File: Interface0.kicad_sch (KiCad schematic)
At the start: 5 parts, among them IC26 MC6821, U107 74LS138, U108 74LS04, U109 74LS11

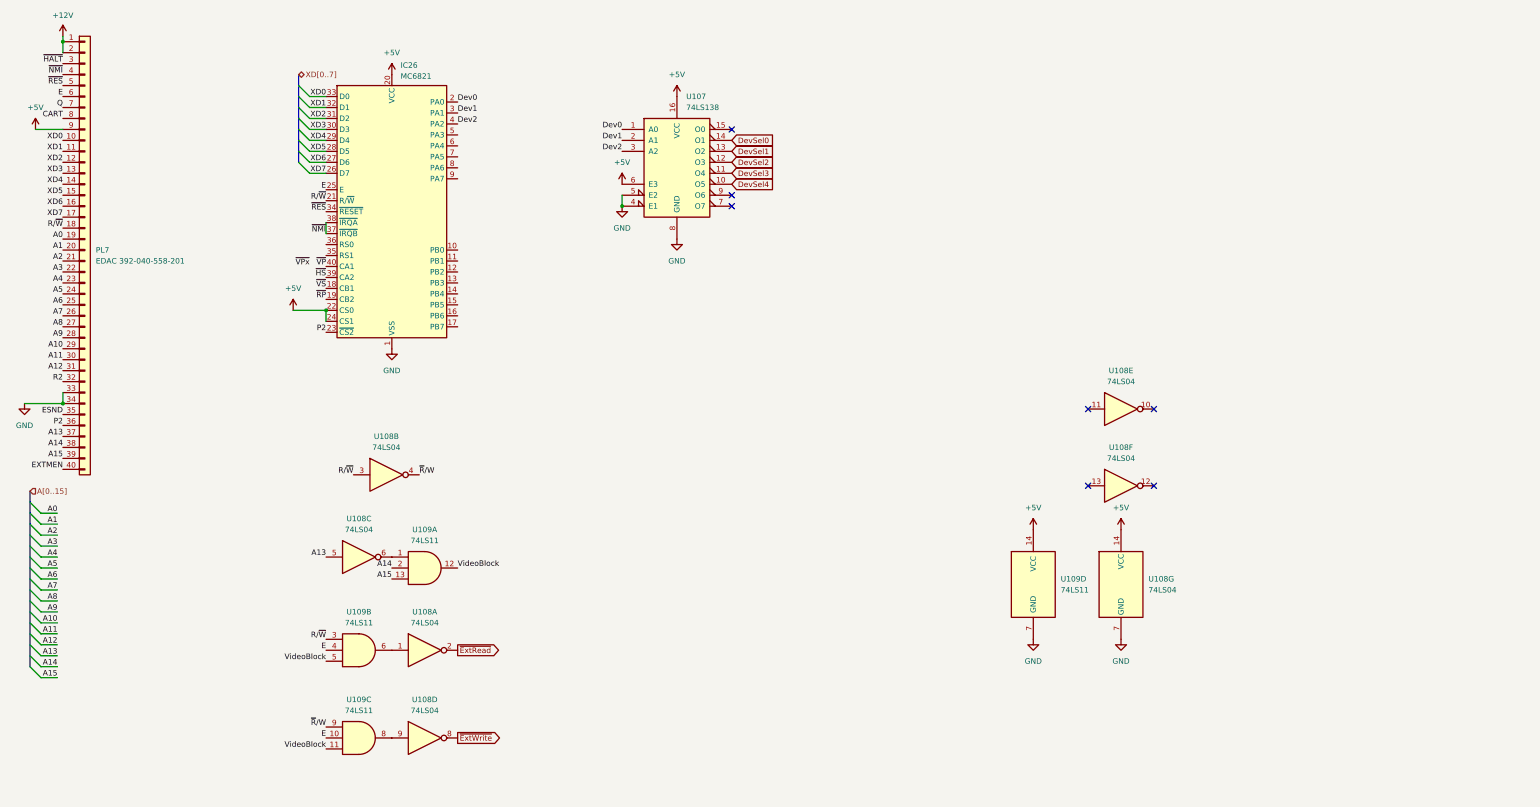
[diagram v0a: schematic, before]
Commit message: refine bus contention solution for host interface
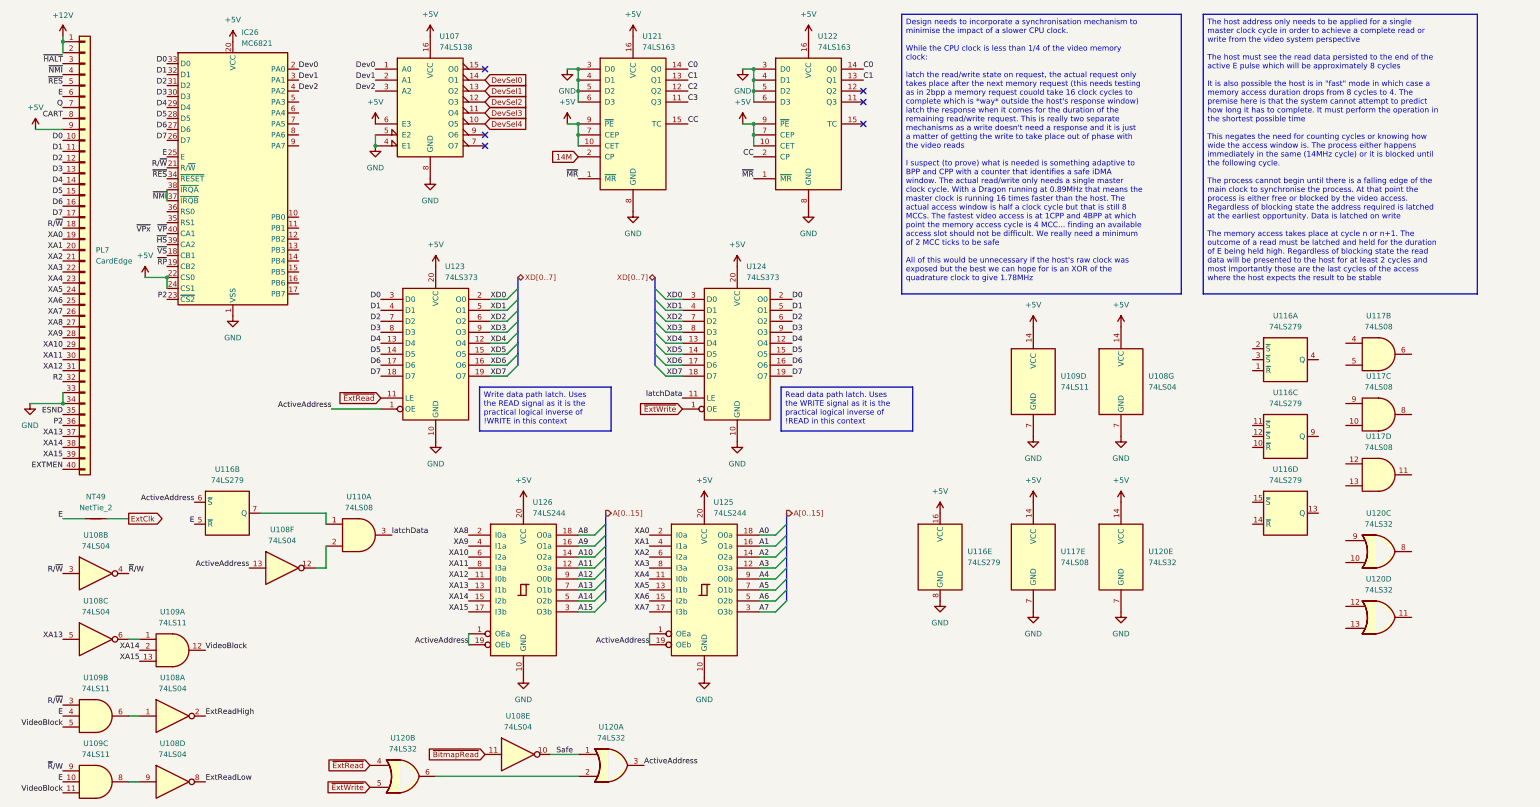
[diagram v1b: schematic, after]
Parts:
- added NT49: NetTie_2, symbol Device:NetTie_2
- added U110, U117: 74LS08, symbol 74xx:74LS08
- added U116: 74LS279, symbol 74xx:74LS279
- added U120: 74LS32, symbol 74xx:74LS32
- added U121, U122: 74LS163, Package_SO:SOIC-16_3.9x9.9mm_P1.27mm, symbol 74xx:74LS163
- added U123, U124: 74LS373, symbol 74xx:74LS373
- added U125, U126: 74LS244, symbol 74xx:74LS244
- PL7: value EDAC 392-040-558-201 -> CardEdge; DigiKey 151-342-040-558-201-ND -> (none); Mouser 587-342-040-558-201 -> (none)
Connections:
- net +5V: now also U116.16 (VCC), U117.14 (VCC), U120.14 (VCC), U121.10 (CET), U121.16 (VCC), U121.7 (CEP), U121.9 (~{PE}), U122.10 (CET), U122.16 (VCC), U122.7 (CEP), U122.9 (~{PE}), U123.20 (VCC), U124.20 (VCC), U125.20 (VCC), U126.20 (VCC)
- net A0: now also U125.18 (O0a); no longer PL7.19 (Pin_19)
- net A1: now also U125.16 (O1a); no longer PL7.20 (Pin_20)
- net A10: now also U126.14 (O2a); no longer PL7.29 (Pin_29)
- net A11: now also U126.12 (O3a); no longer PL7.30 (Pin_30)
- net A12: now also U126.9 (O0b); no longer PL7.31 (Pin_31)
- net A13: now also U126.7 (O1b); no longer PL7.37 (Pin_37), U108.5
- net A14: now also U126.5 (O2b); no longer PL7.38 (Pin_38), U109.2
- net A15: now also U126.3 (O3b); no longer PL7.39 (Pin_39), U109.13
- net A2: now also U125.14 (O2a); no longer PL7.21 (Pin_21)
- net A3: now also U125.12 (O3a); no longer PL7.22 (Pin_22)
- net A4: now also U125.9 (O0b); no longer PL7.23 (Pin_23)
- net A5: now also U125.7 (O1b); no longer PL7.24 (Pin_24)
- net A6: now also U125.5 (O2b); no longer PL7.25 (Pin_25)
- net A7: now also U125.3 (O3b); no longer PL7.26 (Pin_26)
- net A8: now also U126.18 (O0a); no longer PL7.27 (Pin_27)
- net A9: now also U126.16 (O1a); no longer PL7.28 (Pin_28)
- net E: now also NT49.1, U116.5 (~{R})
- net GND: now also U116.8 (GND), U117.7 (GND), U120.7 (GND), U121.3 (D0), U121.4 (D1), U121.5 (D2), U121.6 (D3), U121.8 (GND), U122.3 (D0), U122.4 (D1), U122.5 (D2), U122.6 (D3), U122.8 (GND), U123.10 (GND), U124.10 (GND), U125.10 (GND), U126.10 (GND)
- net XD0: now also U123.2 (O0), U124.3 (D0); no longer IC26.33 (D0), PL7.10 (Pin_10)
- net XD1: now also U123.5 (O1), U124.4 (D1); no longer IC26.32 (D1), PL7.11 (Pin_11)
- net XD2: now also U123.6 (O2), U124.7 (D2); no longer IC26.31 (D2), PL7.12 (Pin_12)
- net XD3: now also U123.9 (O3), U124.8 (D3); no longer IC26.30 (D3), PL7.13 (Pin_13)
- net XD4: now also U123.12 (O4), U124.13 (D4); no longer IC26.29 (D4), PL7.14 (Pin_14)
- net XD5: now also U123.15 (O5), U124.14 (D5); no longer IC26.28 (D5), PL7.15 (Pin_15)
- net XD6: now also U123.16 (O6), U124.17 (D6); no longer IC26.27 (D6), PL7.16 (Pin_16)
- net XD7: now also U123.19 (O7), U124.18 (D7); no longer IC26.26 (D7), PL7.17 (Pin_17)
- net ~{ExtRead}: now also U120.4, U123.11 (LE); no longer U108.2
- net ~{ExtWrite}: now also U120.5, U124.1 (OE); no longer U108.8
- net at U108.12: now also U110.2
- net ActiveAddress: now reaches U108.13
- net ActiveAddress: now also U116.6 (~{S}), U120.3, U123.1 (OE), U125.1 (OEa), U125.19 (OEb), U126.1 (OEa), U126.19 (OEb)
- net Safe: now reaches U108.10
- net Safe: now also U120.1
- net ~{BitmapRead}: now reaches U108.11
- new net: U110.1, U116.7 (Q)
- new net: U120.2, U120.6
- new net 14M: U121.2 (CP)
- new net C0: U121.14 (Q0), U122.14 (Q0)
- new net C1: U121.13 (Q1), U122.13 (Q1)
- new net C2: U121.12 (Q2)
- new net C3: U121.11 (Q3)
- new net CC: U121.15 (TC), U122.2 (CP)
- new net D0: IC26.33 (D0), PL7.10 (Pin_10), U123.3 (D0), U124.2 (O0)
- new net D1: IC26.32 (D1), PL7.11 (Pin_11), U123.4 (D1), U124.5 (O1)
- new net D2: IC26.31 (D2), PL7.12 (Pin_12), U123.7 (D2), U124.6 (O2)
- new net D3: IC26.30 (D3), PL7.13 (Pin_13), U123.8 (D3), U124.9 (O3)
- new net D4: IC26.29 (D4), PL7.14 (Pin_14), U123.13 (D4), U124.12 (O4)
- new net D5: IC26.28 (D5), PL7.15 (Pin_15), U123.14 (D5), U124.15 (O5)
- new net D6: IC26.27 (D6), PL7.16 (Pin_16), U123.17 (D6), U124.16 (O6)
- new net D7: IC26.26 (D7), PL7.17 (Pin_17), U123.18 (D7), U124.19 (O7)
- new net ExtClk: NT49.2
- new net ExtReadHigh: U108.2
- new net ExtReadLow: U108.8
- new net XA0: PL7.19 (Pin_19), U125.2 (I0a)
- new net XA1: PL7.20 (Pin_20), U125.4 (I1a)
- new net XA10: PL7.29 (Pin_29), U126.6 (I2a)
- new net XA11: PL7.30 (Pin_30), U126.8 (I3a)
- new net XA12: PL7.31 (Pin_31), U126.11 (I0b)
- new net XA13: PL7.37 (Pin_37), U108.5, U126.13 (I1b)
- new net XA14: PL7.38 (Pin_38), U109.2, U126.15 (I2b)
- new net XA15: PL7.39 (Pin_39), U109.13, U126.17 (I3b)
- new net XA2: PL7.21 (Pin_21), U125.6 (I2a)
- new net XA3: PL7.22 (Pin_22), U125.8 (I3a)
- new net XA4: PL7.23 (Pin_23), U125.11 (I0b)
- new net XA5: PL7.24 (Pin_24), U125.13 (I1b)
- new net XA6: PL7.25 (Pin_25), U125.15 (I2b)
- new net XA7: PL7.26 (Pin_26), U125.17 (I3b)
- new net XA8: PL7.27 (Pin_27), U126.2 (I0a)
- new net XA9: PL7.28 (Pin_28), U126.4 (I1a)
- new net latchData: U110.3, U124.11 (LE)
- new net ~{MR}: U121.1 (~{MR}), U122.1 (~{MR})
- no-connect marks 7 -> 6
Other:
- moved on the sheet: IC26, U107, U108A, U108B, U108C, U108D, U108E, U108F, U108G, U109A, U109B, U109C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

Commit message: isolate each schematic function for testing
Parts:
- added U90: 74LS08, symbol 74xx:74LS08
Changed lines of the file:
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@@
+	)
+	(symbol
+		(lib_id "74xx:74LS08")
+		(at 307.34 152.4 0)
+		(unit 1)
+		(exclude_from_sim no)
+		(in_bom yes)
+		(on_board yes)
+		(dnp no)
+		(fields_autoplaced yes)
+		(property "Reference" "U90"
+			(at 307.3317 143.51 0)
+			(effects
+				(font
+					(size 1.27 1.27)
+				)
+			)
+		)
+		(property "Value" "74LS08"
+			(at 307.3317 146.05 0)
+			(effects
+				(font
+					(size 1.27 1.27)
+				)
+			)
+		)
+		(property "Footprint" ""
+			(at 307.34 152.4 0)
+			(effects
+				(font
+					(size 1.27 1.27)
+				)
+				(hide yes)
+			)
+		)
+		(property "Datasheet" "http://www.ti.com/lit/gpn/sn74LS08"
+			(at 307.34 152.4 0)
+			(effects
+				(font
+					(size 1.27 1.27)
+				)
+				(hide yes)
+			)
+		)
+		(property "Description" "Quad And2"
+			(at 307.34 152.4 0)
+			(effects
+				(font
+					(size 1.27 1.27)
+				)
+				(hide yes)
+			)
+		)
+		(pin "8"
+		)
+		(pin "4"
+		)
+		(pin "5"
+		)
+		(pin "3"
+		)
+		(pin "10"
+		)
+		(pin "1"
+		)
+		(pin "6"
+		)
+		(pin "2"
+		)
+		(pin "9"
+		)
+		(pin "11"
+		)
+		(pin "14"
+		)
+		(pin "12"
+		)
+		(pin "13"
+		)
+		(pin "7"
+		)
+		(instances
+			(project "DIY-Video"
+				(path "/6c4ef05c-ecf5-4bee-ae4e-d72f13738678/f34f9fb0-9ed6-4c30-921f-18e4206d4b55"
+					(reference "U90")
+					(unit 1)
+				)
+			)
+		)
 	)
 	(symbol

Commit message: spin register out as separate board
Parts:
- removed U110: 74LS08, symbol 74xx:74LS08
- NT49: footprint (none) -> NetTie:NetTie-2_SMD_Pad0.5mm
- PL7: footprint Dragon:Edge_2x20_P2.54mm_OvalMP -> (none)
- U107, U116: footprint (none) -> Package_SO:SOIC-16_3.9x9.9mm_P1.27mm
- U108, U109, U117, U120: footprint (none) -> Package_SO:SO-14_3.9x8.65mm_P1.27mm
- U123, U124, U125, U126: footprint (none) -> Package_SO:SOIC-20W_7.5x12.8mm_P1.27mm
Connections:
- net latchData: now also U117.6
- net at U116.7 (Q): now also U117.4
- net at U108.12: now also U117.5
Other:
- moved on the sheet: U117B
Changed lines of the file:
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@@
 	)
 	(symbol
-		(lib_id "74xx:74LS08")
-		(at 92.71 134.62 0)
-		(unit 1)
-		(exclude_from_sim no)
-		(in_bom yes)
-		(on_board yes)
-		(dnp no)
-		(fields_autoplaced yes)
-		(property "Reference" "U110"
-			(at 92.7017 125.73 0)
-			(effects
-				(font
-					(size 1.27 1.27)
-				)
-			)
-		)
-		(property "Value" "74LS08"
-			(at 92.7017 128.27 0)
-			(effects
-				(font
-					(size 1.27 1.27)
-				)
-			)
-		)
-		(property "Footprint" ""
-			(at 92.71 134.62 0)
-			(effects
-				(font
-					(size 1.27 1.27)
-				)
-				(hide yes)
-			)
-		)
-		(property "Datasheet" "http://www.ti.com/lit/gpn/sn74LS08"
-			(at 92.71 134.62 0)
-			(effects
-				(font
-					(size 1.27 1.27)
-				)
-				(hide yes)
-			)
-		)
-		(property "Description" "Quad And2"
-			(at 92.71 134.62 0)
-			(effects
-				(font
-					(size 1.27 1.27)
-				)
-				(hide yes)
-			)
-		)
-		(pin "9"
-		)
-		(pin "12"
-		)
-		(pin "7"
-		)
-		(pin "14"
-		)
-		(pin "10"
-		)
-		(pin "1"
-		)
-		(pin "6"
-		)
-		(pin "3"
-		)
-		(pin "13"
-		)
-		(pin "4"
-		)
-		(pin "2"
-		)
-		(pin "5"
-		)
-		(pin "11"
-		)
-		(pin "8"
-		)
-		(instances
-			(project "DIY-Video"
-				(path "/6c4ef05c-ecf5-4bee-ae4e-d72f13738678/f34f9fb0-9ed6-4c30-921f-18e4206d4b55"
-					(reference "U110")
-					(unit 1)
-				)
-			)
-		)
-	)
-	(symbol
 		(lib_id "power:+5V")
 		(at 43.18 74.93 0)
@@
 			)
 		)
-		(property "Footprint" ""
+		(property "Footprint" "Package_SO:SOIC-16_3.9x9.9mm_P1.27mm"
 			(at 307.34 111.76 0)
 			(effects
@@
 			)
 		)
-		(property "Footprint" ""
+		(property "Footprint" "Package_SO:SOIC-20W_7.5x12.8mm_P1.27mm"
 			(at 172.72 147.32 0)
 			(effects
@@
 			)
 		)
-		(property "Footprint" ""
+		(property "Footprint" "Package_SO:SO-14_3.9x8.65mm_P1.27mm"
 			(at 49.53 161.29 0)
 			(effects
@@
 			)
 		)
-		(property "Footprint" ""
+		(property "Footprint" "Package_SO:SO-14_3.9x8.65mm_P1.27mm"
 			(at 328.93 106.68 0)
 			(effects
@@
 			)
 		)
-		(property "Footprint" ""
+		(property "Footprint" "Package_SO:SOIC-20W_7.5x12.8mm_P1.27mm"
 			(at 180.34 92.71 0)
 			(effects
@@
 			)
 		)
-		(property "Footprint" ""
+		(property "Footprint" "Package_SO:SOIC-20W_7.5x12.8mm_P1.27mm"
 			(at 130.81 147.32 0)
 			(effects
@@
 			)
 		)
-		(property "Footprint" ""
+		(property "Footprint" "Package_SO:SO-14_3.9x8.65mm_P1.27mm"
 			(at 31.75 143.51 0)
 			(effects
@@
 			)
 		)
-		(property "Footprint" ""
+		(property "Footprint" "Package_SO:SOIC-16_3.9x9.9mm_P1.27mm"
 			(at 227.33 139.7 0)
 			(effects
@@
 			)
 		)
-		(property "Footprint" ""
+		(property "Footprint" "Package_SO:SOIC-16_3.9x9.9mm_P1.27mm"
 			(at 109.22 34.29 0)
 			(effects
@@
 			)
 		)
-		(property "Footprint" ""
+		(property "Footprint" "Package_SO:SO-14_3.9x8.65mm_P1.27mm"
 			(at 74.93 142.24 0)
 			(effects
@@
 			)
 		)
-		(property "Footprint" ""
+		(property "Footprint" "Package_SO:SOIC-20W_7.5x12.8mm_P1.27mm"
 			(at 110.49 92.71 0)
 			(effects
@@
 			)
 		)
-		(property "Footprint" ""
+		(property "Footprint" "Package_SO:SO-14_3.9x8.65mm_P1.27mm"
 			(at 269.24 139.7 0)
 			(effects
@@
 			)
 		)
-		(property "Footprint" ""
+		(property "Footprint" "Package_SO:SO-14_3.9x8.65mm_P1.27mm"
 			(at 328.93 138.43 0)
 			(effects
@@
 			)
 		)
-		(property "Footprint" ""
+		(property "Footprint" "Package_SO:SOIC-16_3.9x9.9mm_P1.27mm"
 			(at 307.34 129.54 0)
 			(effects
@@
 			)
 		)
-		(property "Footprint" ""
+		(property "Footprint" "Package_SO:SO-14_3.9x8.65mm_P1.27mm"
 			(at 31.75 158.75 0)
 			(effects
@@
 			)
 		)
-		(property "Footprint" ""
+		(property "Footprint" "Package_SO:SO-14_3.9x8.65mm_P1.27mm"
 			(at 248.92 139.7 0)
 			(effects
@@
 			)
 		)
-		(property "Footprint" ""
+		(property "Footprint" "Package_SO:SO-14_3.9x8.65mm_P1.27mm"
 			(at 328.93 153.67 0)
 			(effects
@@
 			)
 		)
-		(property "Footprint" ""
+		(property "Footprint" "Package_SO:SO-14_3.9x8.65mm_P1.27mm"
 			(at 31.75 176.53 0)
 			(effects
@@
 			)
 		)
-		(property "Footprint" ""
+		(property "Footprint" "NetTie:NetTie-2_SMD_Pad0.5mm"
 			(at 31.75 130.81 0)
 			(effects
@@
 			)
 		)
-		(property "Footprint" ""
+		(property "Footprint" "Package_SO:SO-14_3.9x8.65mm_P1.27mm"
 			(at 102.87 190.5 0)
 			(effects
@@
 			)
 		)
-		(property "Footprint" ""
+		(property "Footprint" "Package_SO:SOIC-16_3.9x9.9mm_P1.27mm"
 			(at 62.23 129.54 0)
 			(effects
@@
 			)
 		)
-		(property "Footprint" ""
+		(property "Footprint" "Package_SO:SO-14_3.9x8.65mm_P1.27mm"
 			(at 49.53 176.53 0)
 			(effects
@@
 			)
 		)
-		(property "Footprint" ""
+		(property "Footprint" "Package_SO:SO-14_3.9x8.65mm_P1.27mm"
 			(at 328.93 120.65 0)
 			(effects
@@
 			)
 		)
-		(property "Footprint" ""
+		(property "Footprint" "Package_SO:SO-14_3.9x8.65mm_P1.27mm"
 			(at 49.53 191.77 0)
 			(effects
@@
 			)
 		)
-		(property "Footprint" "Dragon:Edge_2x20_P2.54mm_OvalMP"
+		(property "Footprint" ""
 			(at 29.21 68.58 0)
 			(effects
@@
 			)
 		)
-		(property "Footprint" ""
+		(property "Footprint" "Package_SO:SO-14_3.9x8.65mm_P1.27mm"
 			(at 129.54 185.42 0)
 			(effects
@@
 			)
 		)
-		(property "Footprint" ""
+		(property "Footprint" "Package_SO:SO-14_3.9x8.65mm_P1.27mm"
 			(at 269.24 99.06 0)
 			(effects
@@
 			)
 		)
-		(property "Footprint" ""
+		(property "Footprint" "Package_SO:SO-14_3.9x8.65mm_P1.27mm"
 			(at 151.13 187.96 0)
 			(effects
@@
 			)
 		)
-		(property "Footprint" ""
+		(property "Footprint" "Package_SO:SOIC-16_3.9x9.9mm_P1.27mm"
 			(at 307.34 93.98 0)
 			(effects
@@
 			)
 		)
-		(property "Footprint" ""
+		(property "Footprint" "Package_SO:SO-14_3.9x8.65mm_P1.27mm"
 			(at 248.92 99.06 0)
 			(effects
@@
 	(symbol
 		(lib_id "74xx:74LS08")
-		(at 328.93 92.71 0)
+		(at 92.71 134.62 0)
 		(unit 2)
 		(exclude_from_sim no)
@@
 		(fields_autoplaced yes)
 		(property "Reference" "U117"
-			(at 328.9217 83.82 0)
+			(at 92.7017 125.73 0)
 			(effects
 				(font
@@
 		)
 		(property "Value" "74LS08"
-			(at 328.9217 86.36 0)
+			(at 92.7017 128.27 0)
 			(effects
 				(font
@@
 			)
 		)
-		(property "Footprint" ""
-			(at 328.93 92.71 0)
+		(property "Footprint" "Package_SO:SO-14_3.9x8.65mm_P1.27mm"
+			(at 92.71 134.62 0)
 			(effects
 				(font
@@
 		)
 		(property "Datasheet" "http://www.ti.com/lit/gpn/sn74LS08"
-			(at 328.93 92.71 0)
+			(at 92.71 134.62 0)
 			(effects
 				(font
@@
 		)
 		(property "Description" "Quad And2"
-			(at 328.93 92.71 0)
+			(at 92.71 134.62 0)
 			(effects
 				(font
@@
 			)
 		)
-		(property "Footprint" ""
+		(property "Footprint" "Package_SO:SO-14_3.9x8.65mm_P1.27mm"
 			(at 31.75 191.77 0)
 			(effects
